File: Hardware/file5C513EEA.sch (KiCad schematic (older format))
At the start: 87 parts, among them J10 IN_2, J11 IN_3, J12 PWM_CV, J13 EXT_CON, J4 OUT2_CON, J5 CUTOFF_CV, J6 SHAPE_CV, J7 SET_CV, J8 OUT1_CON, J9 IN_1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

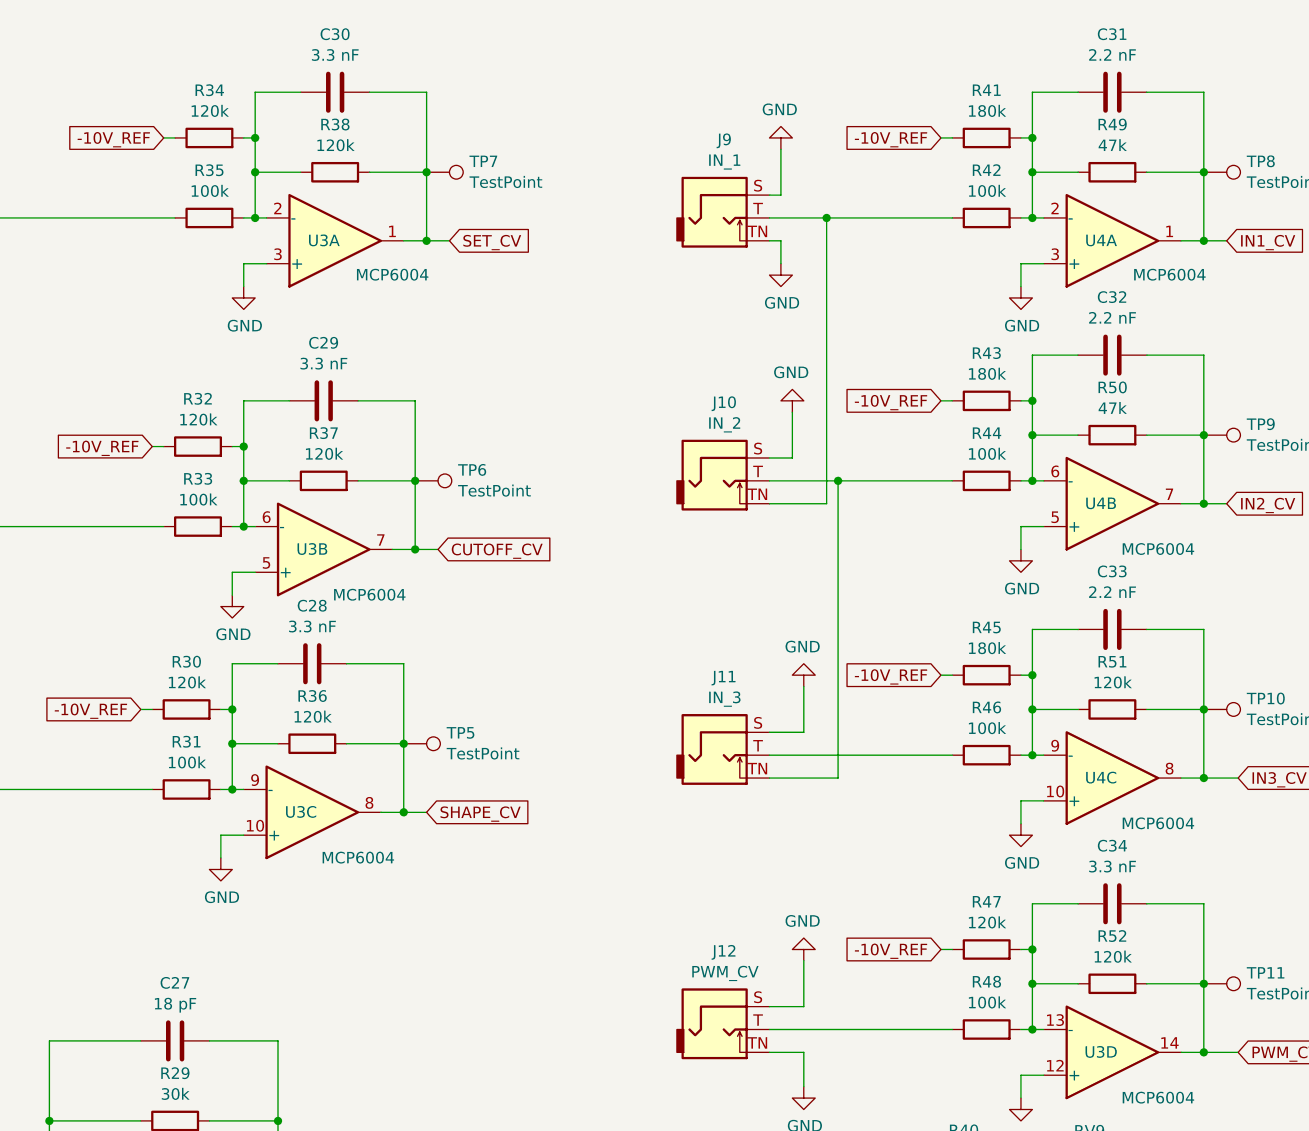
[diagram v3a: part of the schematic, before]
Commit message: Finalized 4 layer design, fixed bad opamp circuits
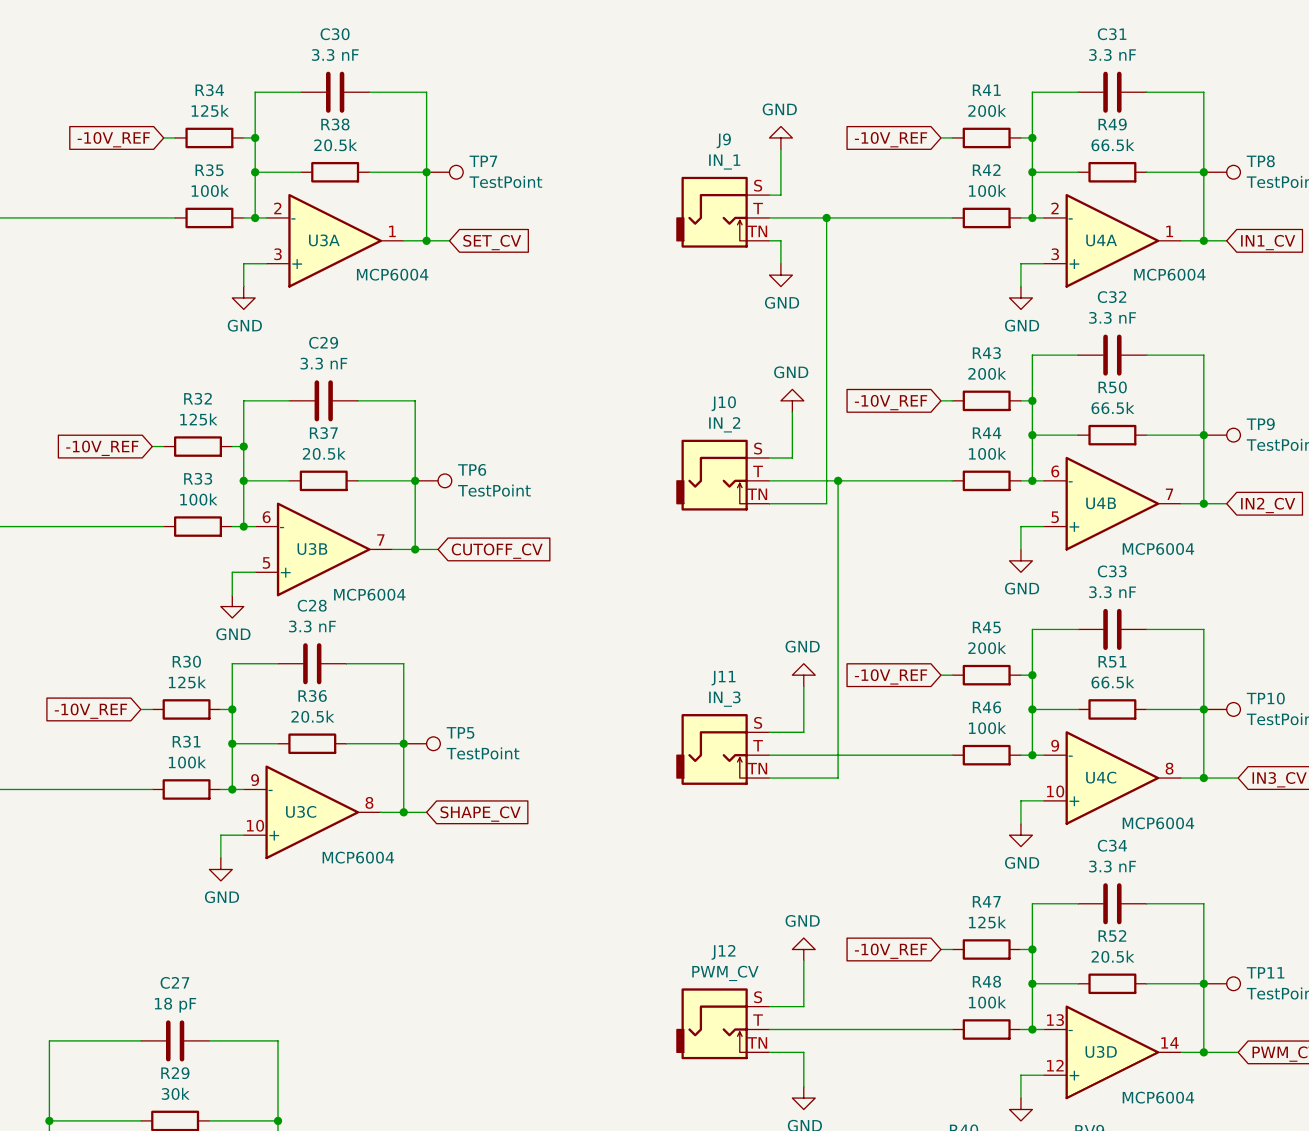
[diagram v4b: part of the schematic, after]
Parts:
- C31, C32, C33: value 2.2 nF -> 3.3 nF
- R30, R32, R34, R47: value 120k -> 125k
- R36, R37, R38, R52: value 120k -> 20.5k
- R41, R43, R45: value 180k -> 200k
- R49, R50: value 47k -> 66.5k
- R51: value 120k -> 66.5k
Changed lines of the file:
@@
 AR Path="/5BFD63E3/5C513EEB/5C5CD2AF" Ref="R41"  Part="1"
 F 0 "R41" V 9807 1050 50  0000 C CNN
-F 1 "180k" V 9716 1050 50  0000 C CNN
+F 1 "200k" V 9716 1050 50  0000 C CNN
 F 2 "Resistor_SMD:R_0603_1608Metric" V 9530 1050 50  0001 C CNN
 F 3 "~" H 9600 1050 50  0001 C CNN
@@
 AR Path="/5BFD63E3/5C513EEB/5C5CD2B6" Ref="R49"  Part="1"
 F 0 "R49" V 10357 1200 50  0000 C CNN
-F 1 "47k" V 10266 1200 50  0000 C CNN
+F 1 "66.5k" V 10266 1200 50  0000 C CNN
 F 2 "Resistor_SMD:R_0603_1608Metric" V 10080 1200 50  0001 C CNN
 F 3 "~" H 10150 1200 50  0001 C CNN
@@
 AR Path="/5BFD63E3/5C513EEB/5C5CD2BE" Ref="C31"  Part="1"
 F 0 "C31" V 9898 850 50  0000 C CNN
-F 1 "2.2 nF" V 9989 850 50  0000 C CNN
+F 1 "3.3 nF" V 9989 850 50  0000 C CNN
 F 2 "Capacitor_SMD:C_0603_1608Metric" H 10188 700 50  0001 C CNN
 F 3 "~" H 10150 850 50  0001 C CNN
@@
 AR Path="/5BFD63E3/5C513EEB/5C5CD2F9" Ref="R43"  Part="1"
 F 0 "R43" V 9807 2200 50  0000 C CNN
-F 1 "180k" V 9716 2200 50  0000 C CNN
+F 1 "200k" V 9716 2200 50  0000 C CNN
 F 2 "Resistor_SMD:R_0603_1608Metric" V 9530 2200 50  0001 C CNN
 F 3 "~" H 9600 2200 50  0001 C CNN
@@
 AR Path="/5BFD63E3/5C513EEB/5C5CD300" Ref="R50"  Part="1"
 F 0 "R50" V 10357 2350 50  0000 C CNN
-F 1 "47k" V 10266 2350 50  0000 C CNN
+F 1 "66.5k" V 10266 2350 50  0000 C CNN
 F 2 "Resistor_SMD:R_0603_1608Metric" V 10080 2350 50  0001 C CNN
 F 3 "~" H 10150 2350 50  0001 C CNN
@@
 AR Path="/5BFD63E3/5C513EEB/5C5CD308" Ref="C32"  Part="1"
 F 0 "C32" V 9898 2000 50  0000 C CNN
-F 1 "2.2 nF" V 9989 2000 50  0000 C CNN
+F 1 "3.3 nF" V 9989 2000 50  0000 C CNN
 F 2 "Capacitor_SMD:C_0603_1608Metric" H 10188 1850 50  0001 C CNN
 F 3 "~" H 10150 2000 50  0001 C CNN
@@
 AR Path="/5BFD63E3/5C513EEB/5C5CD343" Ref="R45"  Part="1"
 F 0 "R45" V 9807 3400 50  0000 C CNN
-F 1 "180k" V 9716 3400 50  0000 C CNN
+F 1 "200k" V 9716 3400 50  0000 C CNN
 F 2 "Resistor_SMD:R_0603_1608Metric" V 9530 3400 50  0001 C CNN
 F 3 "~" H 9600 3400 50  0001 C CNN
@@
 AR Path="/5BFD63E3/5C513EEB/5C5CD34A" Ref="R51"  Part="1"
 F 0 "R51" V 10357 3550 50  0000 C CNN
-F 1 "120k" V 10266 3550 50  0000 C CNN
+F 1 "66.5k" V 10266 3550 50  0000 C CNN
 F 2 "Resistor_SMD:R_0603_1608Metric" V 10080 3550 50  0001 C CNN
 F 3 "~" H 10150 3550 50  0001 C CNN
@@
 AR Path="/5BFD63E3/5C513EEB/5C5CD352" Ref="C33"  Part="1"
 F 0 "C33" V 9898 3200 50  0000 C CNN
-F 1 "2.2 nF" V 9989 3200 50  0000 C CNN
+F 1 "3.3 nF" V 9989 3200 50  0000 C CNN
 F 2 "Capacitor_SMD:C_0603_1608Metric" H 10188 3050 50  0001 C CNN
 F 3 "~" H 10150 3200 50  0001 C CNN
@@
 AR Path="/5BFD63E3/5C513EEB/5C5CD38C" Ref="R47"  Part="1"
 F 0 "R47" V 9807 4600 50  0000 C CNN
-F 1 "120k" V 9716 4600 50  0000 C CNN
+F 1 "125k" V 9716 4600 50  0000 C CNN
 F 2 "Resistor_SMD:R_0603_1608Metric" V 9530 4600 50  0001 C CNN
 F 3 "~" H 9600 4600 50  0001 C CNN
@@
 AR Path="/5BFD63E3/5C513EEB/5C5CD393" Ref="R52"  Part="1"
 F 0 "R52" V 10357 4750 50  0000 C CNN
-F 1 "120k" V 10266 4750 50  0000 C CNN
+F 1 "20.5k" V 10266 4750 50  0000 C CNN
 F 2 "Resistor_SMD:R_0603_1608Metric" V 10080 4750 50  0001 C CNN
 F 3 "~" H 10150 4750 50  0001 C CNN
@@
 AR Path="/5BFD63E3/5C513EEB/5C5D98E3" Ref="R32"  Part="1"
 F 0 "R32" V 6357 2400 50  0000 C CNN
-F 1 "120k" V 6266 2400 50  0000 C CNN
+F 1 "125k" V 6266 2400 50  0000 C CNN
 F 2 "Resistor_SMD:R_0603_1608Metric" V 6080 2400 50  0001 C CNN
 F 3 "~" H 6150 2400 50  0001 C CNN
@@
 AR Path="/5BFD63E3/5C513EEB/5C5D98EA" Ref="R37"  Part="1"
 F 0 "R37" V 6907 2550 50  0000 C CNN
-F 1 "120k" V 6816 2550 50  0000 C CNN
+F 1 "20.5k" V 6816 2550 50  0000 C CNN
 F 2 "Resistor_SMD:R_0603_1608Metric" V 6630 2550 50  0001 C CNN
 F 3 "~" H 6700 2550 50  0001 C CNN
@@
 AR Path="/5BFD63E3/5C513EEB/5C5D9921" Ref="R30"  Part="1"
 F 0 "R30" V 6307 3550 50  0000 C CNN
-F 1 "120k" V 6216 3550 50  0000 C CNN
+F 1 "125k" V 6216 3550 50  0000 C CNN
 F 2 "Resistor_SMD:R_0603_1608Metric" V 6030 3550 50  0001 C CNN
 F 3 "~" H 6100 3550 50  0001 C CNN
@@
 AR Path="/5BFD63E3/5C513EEB/5C5D9928" Ref="R36"  Part="1"
 F 0 "R36" V 6857 3700 50  0000 C CNN
-F 1 "120k" V 6766 3700 50  0000 C CNN
+F 1 "20.5k" V 6766 3700 50  0000 C CNN
 F 2 "Resistor_SMD:R_0603_1608Metric" V 6580 3700 50  0001 C CNN
 F 3 "~" H 6650 3700 50  0001 C CNN
@@
 AR Path="/5BFD63E3/5C513EEB/5BE21E92" Ref="R34"  Part="1"
 F 0 "R34" V 6407 1050 50  0000 C CNN
-F 1 "120k" V 6316 1050 50  0000 C CNN
+F 1 "125k" V 6316 1050 50  0000 C CNN
 F 2 "Resistor_SMD:R_0603_1608Metric" V 6130 1050 50  0001 C CNN
 F 3 "~" H 6200 1050 50  0001 C CNN
@@
 AR Path="/5BFD63E3/5C513EEB/5BE21E99" Ref="R38"  Part="1"
 F 0 "R38" V 6957 1200 50  0000 C CNN
-F 1 "120k" V 6866 1200 50  0000 C CNN
+F 1 "20.5k" V 6866 1200 50  0000 C CNN
 F 2 "Resistor_SMD:R_0603_1608Metric" V 6680 1200 50  0001 C CNN
 F 3 "~" H 6750 1200 50  0001 C CNN

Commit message: Finished design of 4 layer, added stero option and logo
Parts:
- added J18: Conn_01x02_Male, Connector_JST:JST_PH_B2B-PH-K_1x02_P2.00mm_Vertical, symbol Connector:Conn_01x02_Male
- added JP2: SolderJumper_3_Bridged12, Jumper:SolderJumper-3_P1.3mm_Bridged12_RoundedPad1.0x1.5mm_NumberLabels, symbol Jumper:SolderJumper_3_Bridged12
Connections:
- net GND: now also J18.2 (Pin_2)
- net SID_OUT: now also JP2.1 (A); no longer U2.5 (+)
- new net: JP2.2 (C), U2.5 (+)
- new net: J18.1 (Pin_1), JP2.3 (B)
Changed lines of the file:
@@
 Wire Wire Line
 	5350 5550 5750 5550
-Text GLabel 1100 6900 0    50   Input ~ 0
+Text GLabel 850  7600 0    50   Input ~ 0
 SID_OUT
 $Comp
@@
 Wire Wire Line
 	3000 7100 3150 7100
-Wire Wire Line
-	1100 6900 1500 6900
 $Comp
 L Device:R R?
@@
 Wire Wire Line
 	5450 6950 5450 7050
-Wire Wire Line
-	1250 7550 1250 7450
 $Comp
 L Amplifier_Operational:MCP6002-xSN U?
@@
 	0    1    1    0
 $EndComp
+$Comp
+L Connector:Conn_01x02_Male J?
+U 1 1 5CA018EC
+P 800 6400
+AR Path="/5C5AA76E/5CA018EC" Ref="J?"  Part="1"
+AR Path="/5BFD63E3/5C513EEB/5CA018EC" Ref="J18"  Part="1"
+F 0 "J18" V 860 6213 50  0000 R CNN
+F 1 "Conn_01x02_Male" V 951 6213 50  0000 R CNN
+F 2 "Connector_JST:JST_PH_B2B-PH-K_1x02_P2.00mm_Vertical" H 800 6400 50  0001 C CNN
+F 3 "~" H 800 6400 50  0001 C CNN
+	1    800  6400
+	0    -1   1    0
+$EndComp
+$Comp
+L Jumper:SolderJumper_3_Bridged12 JP2
+U 1 1 5CA38124
+P 750 7250
+F 0 "JP2" H 750 7362 50  0000 C CNN
+F 1 "SolderJumper_3_Bridged12" H 750 7453 50  0000 C CNN
+F 2 "Jumper:SolderJumper-3_P1.3mm_Bridged12_RoundedPad1.0x1.5mm_NumberLabels" H 750 7250 50  0001 C CNN
+F 3 "~" H 750 7250 50  0001 C CNN
+	1    750  7250
+	-1   0    0    1
+$EndComp
+$Comp
+L power:GND #PWR0188
+U 1 1 5CABE347
+P 900 6700
+F 0 "#PWR0188" H 900 6450 50  0001 C CNN
+F 1 "GND" H 905 6527 50  0000 C CNN
+F 2 "" H 900 6700 50  0001 C CNN
+F 3 "" H 900 6700 50  0001 C CNN
+	1    900  6700
+	1    0    0    -1
+$EndComp
+Wire Wire Line
+	900  6700 900  6600
+Wire Wire Line
+	1250 7450 1250 7550
+Wire Wire Line
+	750  6900 750  7100
+Wire Wire Line
+	750  6900 1500 6900
+Wire Wire Line
+	850  7600 1000 7600
+Wire Wire Line
+	1000 7600 1000 7250
+Wire Wire Line
+	1000 7250 950  7250
+Wire Wire Line
+	550  7250 550  6600
+Wire Wire Line
+	550  6600 800  6600
 $EndSCHEMATC

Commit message: Started state machine
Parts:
- added R? (x2): 1k, Resistor_SMD:R_0603_1608Metric, symbol Device:R
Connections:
- net GND: now also R?.2, R?.2
- net SID_OUT: now also R?.1
- net at JP2.2 (C), U2.5 (+): now also R?.1
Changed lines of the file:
@@
 Wire Wire Line
 	7100 5750 7150 5750
-Text GLabel 5350 5550 0    50   Input ~ 0
+Text GLabel 4850 5550 0    50   Input ~ 0
 SID_OUT
 Wire Wire Line
-	5350 5550 5750 5550
+	4850 5550 5150 5550
 Text GLabel 850  7600 0    50   Input ~ 0
 SID_OUT
@@
 L power:GND #PWR?
 U 1 1 5C59381E
-P 5500 6100
+P 5300 6200
 AR Path="/5BFD63E3/5C59381E" Ref="#PWR?"  Part="1"
 AR Path="/5BFD63E3/5C513EEB/5C59381E" Ref="#PWR086"  Part="1"
-F 0 "#PWR086" H 5500 5850 50  0001 C CNN
-F 1 "GND" H 5505 5927 50  0000 C CNN
-F 2 "" H 5500 6100 50  0001 C CNN
-F 3 "" H 5500 6100 50  0001 C CNN
-	1    5500 6100
+F 0 "#PWR086" H 5300 5950 50  0001 C CNN
+F 1 "GND" H 5305 6027 50  0000 C CNN
+F 2 "" H 5300 6200 50  0001 C CNN
+F 3 "" H 5300 6200 50  0001 C CNN
+	1    5300 6200
 	1    0    0    -1
 $EndComp
@@
 	900  6700 900  6600
 Wire Wire Line
-	1250 7450 1250 7550
+	1250 7450 1250 7500
 Wire Wire Line
 	750  6900 750  7100
 Wire Wire Line
-	750  6900 1500 6900
+	750  6900 1000 6900
 Wire Wire Line
 	850  7600 1000 7600
@@
 Wire Wire Line
 	550  6600 800  6600
+$Comp
+L Device:R R?
+U 1 1 5CBC072D
+P 5150 5950
+AR Path="/5BFD63E3/5CBC072D" Ref="R?"  Part="1"
+AR Path="/5BFD63E3/5C513EEB/5CBC072D" Ref="R?"  Part="1"
+F 0 "R?" V 5357 5950 50  0000 C CNN
+F 1 "1k" V 5266 5950 50  0000 C CNN
+F 2 "Resistor_SMD:R_0603_1608Metric" V 5080 5950 50  0001 C CNN
+F 3 "~" H 5150 5950 50  0001 C CNN
+	1    5150 5950
+	1    0    0    -1
+$EndComp
+Wire Wire Line
+	5150 5800 5150 5550
+Connection ~ 5150 5550
+Wire Wire Line
+	5150 5550 5750 5550
+Wire Wire Line
+	5300 6200 5300 6100
+Wire Wire Line
+	5300 6100 5150 6100
+Wire Wire Line
+	5500 6100 5300 6100
+Connection ~ 5300 6100
+$Comp
+L Device:R R?
+U 1 1 5CC4C9FE
+P 1000 7050
+AR Path="/5BFD63E3/5CC4C9FE" Ref="R?"  Part="1"
+AR Path="/5BFD63E3/5C513EEB/5CC4C9FE" Ref="R?"  Part="1"
+F 0 "R?" V 1207 7050 50  0000 C CNN
+F 1 "1k" V 1116 7050 50  0000 C CNN
+F 2 "Resistor_SMD:R_0603_1608Metric" V 930 7050 50  0001 C CNN
+F 3 "~" H 1000 7050 50  0001 C CNN
+	1    1000 7050
+	1    0    0    -1
+$EndComp
+Connection ~ 1000 6900
+Wire Wire Line
+	1000 6900 1500 6900
+Wire Wire Line
+	1000 7200 1150 7200
+Wire Wire Line
+	1150 7200 1150 7500
+Wire Wire Line
+	1150 7500 1250 7500
+Connection ~ 1250 7500
+Wire Wire Line
+	1250 7500 1250 7550
 $EndSCHEMATC

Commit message: More work
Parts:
- R30, R32, R34, R47: value 125k -> 124k
- R41, R43, R45: value 200k -> 124k
- R49, R50, R51: value 66.5k -> 39k
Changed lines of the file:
@@
 AR Path="/5BFD63E3/5C513EEB/5C5CD2AF" Ref="R41"  Part="1"
 F 0 "R41" V 9807 1050 50  0000 C CNN
-F 1 "200k" V 9716 1050 50  0000 C CNN
+F 1 "124k" V 9716 1050 50  0000 C CNN
 F 2 "Resistor_SMD:R_0603_1608Metric" V 9530 1050 50  0001 C CNN
 F 3 "~" H 9600 1050 50  0001 C CNN
@@
 AR Path="/5BFD63E3/5C513EEB/5C5CD2B6" Ref="R49"  Part="1"
 F 0 "R49" V 10357 1200 50  0000 C CNN
-F 1 "66.5k" V 10266 1200 50  0000 C CNN
+F 1 "39k" V 10266 1200 50  0000 C CNN
 F 2 "Resistor_SMD:R_0603_1608Metric" V 10080 1200 50  0001 C CNN
 F 3 "~" H 10150 1200 50  0001 C CNN
@@
 AR Path="/5BFD63E3/5C513EEB/5C5CD2F9" Ref="R43"  Part="1"
 F 0 "R43" V 9807 2200 50  0000 C CNN
-F 1 "200k" V 9716 2200 50  0000 C CNN
+F 1 "124k" V 9716 2200 50  0000 C CNN
 F 2 "Resistor_SMD:R_0603_1608Metric" V 9530 2200 50  0001 C CNN
 F 3 "~" H 9600 2200 50  0001 C CNN
@@
 AR Path="/5BFD63E3/5C513EEB/5C5CD300" Ref="R50"  Part="1"
 F 0 "R50" V 10357 2350 50  0000 C CNN
-F 1 "66.5k" V 10266 2350 50  0000 C CNN
+F 1 "39k" V 10266 2350 50  0000 C CNN
 F 2 "Resistor_SMD:R_0603_1608Metric" V 10080 2350 50  0001 C CNN
 F 3 "~" H 10150 2350 50  0001 C CNN
@@
 AR Path="/5BFD63E3/5C513EEB/5C5CD343" Ref="R45"  Part="1"
 F 0 "R45" V 9807 3400 50  0000 C CNN
-F 1 "200k" V 9716 3400 50  0000 C CNN
+F 1 "124k" V 9716 3400 50  0000 C CNN
 F 2 "Resistor_SMD:R_0603_1608Metric" V 9530 3400 50  0001 C CNN
 F 3 "~" H 9600 3400 50  0001 C CNN
@@
 AR Path="/5BFD63E3/5C513EEB/5C5CD34A" Ref="R51"  Part="1"
 F 0 "R51" V 10357 3550 50  0000 C CNN
-F 1 "66.5k" V 10266 3550 50  0000 C CNN
+F 1 "39k" V 10266 3550 50  0000 C CNN
 F 2 "Resistor_SMD:R_0603_1608Metric" V 10080 3550 50  0001 C CNN
 F 3 "~" H 10150 3550 50  0001 C CNN
@@
 AR Path="/5BFD63E3/5C513EEB/5C5CD38C" Ref="R47"  Part="1"
 F 0 "R47" V 9807 4600 50  0000 C CNN
-F 1 "125k" V 9716 4600 50  0000 C CNN
+F 1 "124k" V 9716 4600 50  0000 C CNN
 F 2 "Resistor_SMD:R_0603_1608Metric" V 9530 4600 50  0001 C CNN
 F 3 "~" H 9600 4600 50  0001 C CNN
@@
 AR Path="/5BFD63E3/5C513EEB/5C5D98E3" Ref="R32"  Part="1"
 F 0 "R32" V 6357 2400 50  0000 C CNN
-F 1 "125k" V 6266 2400 50  0000 C CNN
+F 1 "124k" V 6266 2400 50  0000 C CNN
 F 2 "Resistor_SMD:R_0603_1608Metric" V 6080 2400 50  0001 C CNN
 F 3 "~" H 6150 2400 50  0001 C CNN
@@
 AR Path="/5BFD63E3/5C513EEB/5C5D9921" Ref="R30"  Part="1"
 F 0 "R30" V 6307 3550 50  0000 C CNN
-F 1 "125k" V 6216 3550 50  0000 C CNN
+F 1 "124k" V 6216 3550 50  0000 C CNN
 F 2 "Resistor_SMD:R_0603_1608Metric" V 6030 3550 50  0001 C CNN
 F 3 "~" H 6100 3550 50  0001 C CNN
@@
 AR Path="/5BFD63E3/5C513EEB/5BE21E92" Ref="R34"  Part="1"
 F 0 "R34" V 6407 1050 50  0000 C CNN
-F 1 "125k" V 6316 1050 50  0000 C CNN
+F 1 "124k" V 6316 1050 50  0000 C CNN
 F 2 "Resistor_SMD:R_0603_1608Metric" V 6130 1050 50  0001 C CNN
 F 3 "~" H 6200 1050 50  0001 C CNN
